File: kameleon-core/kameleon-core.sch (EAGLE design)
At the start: 38 parts, among them CN1 USB, CN3 LEFT, CN4 RIGHT, CN5 SWD, IC3 STM32F411CE/UFQFPN48, IC4 AP2112K-3.3TRG1, SW1 NRST, SW2 BTN, Y1 8MHz

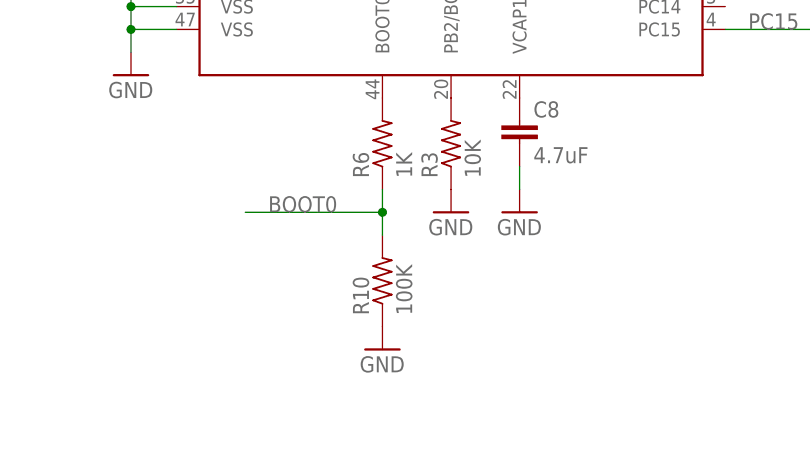
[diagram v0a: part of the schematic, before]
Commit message: Change R10 value to 10K
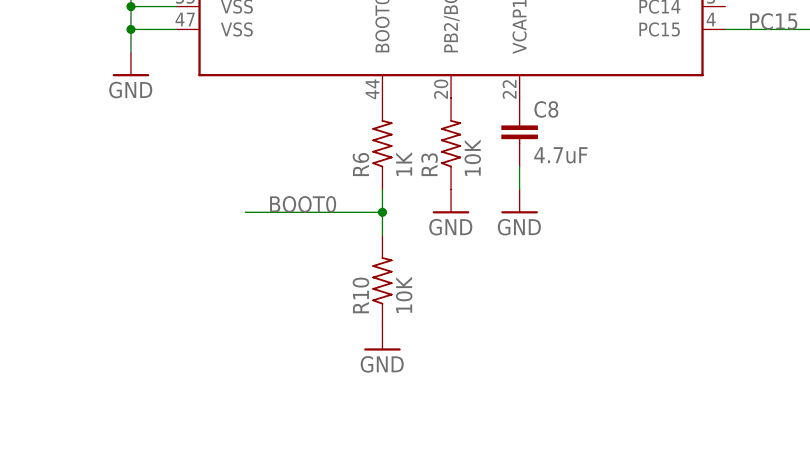
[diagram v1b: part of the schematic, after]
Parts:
- R10: value 100K -> 10K
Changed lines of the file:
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@@
 <part name="+3V1" library="supply1" deviceset="+3V3" device=""/>
 <part name="R6" library="Kameleon" deviceset="RES" device="" value="1K"/>
-<part name="R10" library="Kameleon" deviceset="RES" device="" value="100K"/>
+<part name="R10" library="Kameleon" deviceset="RES" device="" value="10K"/>
 <part name="GND2" library="supply1" deviceset="GND" device=""/>
 <part name="R3" library="Kameleon" deviceset="RES" device="" value="10K"/>

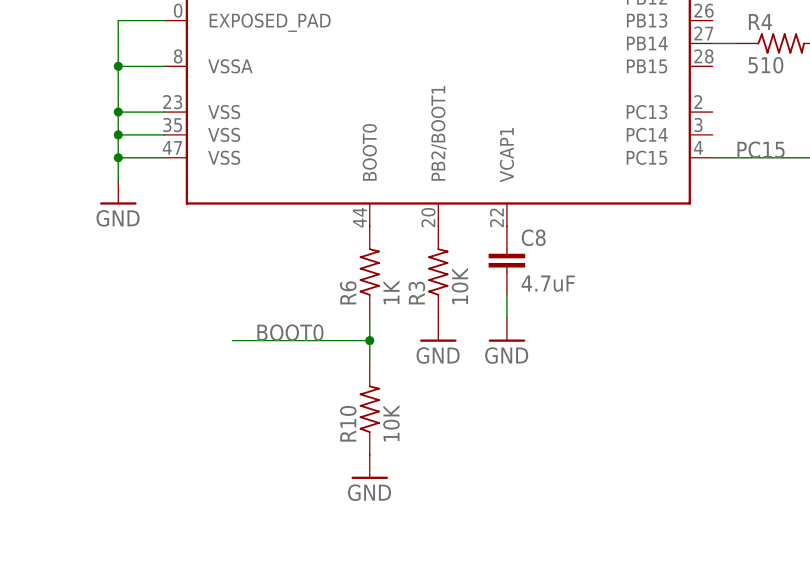
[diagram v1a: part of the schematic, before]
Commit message: Remove R3 and R6 because it's not needed
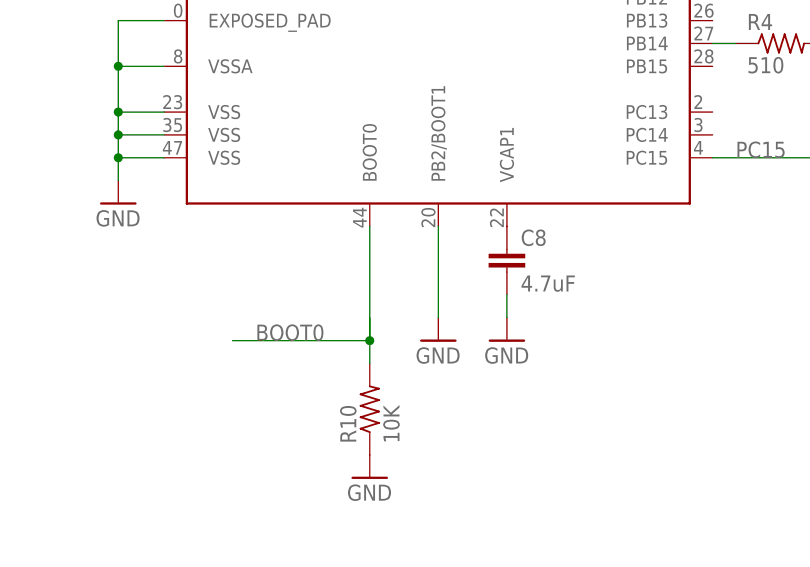
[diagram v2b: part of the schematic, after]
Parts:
- removed R3: 10K, Kameleon:RES
- removed R6: 1K, Kameleon:RES
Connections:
- removed net N$1: IC3.BOOT0, R6.2
- removed net N$2: IC3.PB2/BOOT1, R3.2
- net BOOT0: now also IC3.BOOT0; no longer R6.1
- net GND: now also IC3.PB2/BOOT1; no longer R3.1
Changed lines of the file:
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@@
 <part name="GND1" library="supply1" deviceset="GND" device=""/>
 <part name="+3V1" library="supply1" deviceset="+3V3" device=""/>
-<part name="R6" library="Kameleon" deviceset="RES" device="" value="1K"/>
 <part name="R10" library="Kameleon" deviceset="RES" device="" value="10K"/>
 <part name="GND2" library="supply1" deviceset="GND" device=""/>
-<part name="R3" library="Kameleon" deviceset="RES" device="" value="10K"/>
 <part name="GND3" library="supply1" deviceset="GND" device=""/>
 <part name="GND4" library="supply1" deviceset="GND" device=""/>
@@
 <attribute name="VALUE" x="38.1" y="134.62" size="1.778" layer="96" rot="R90"/>
 </instance>
-<instance part="R6" gate="G$1" x="68.58" y="35.56" smashed="yes" rot="R90">
-<attribute name="NAME" x="67.0814" y="31.75" size="1.778" layer="95" rot="R90"/>
-<attribute name="VALUE" x="71.882" y="31.75" size="1.778" layer="96" rot="R90"/>
-</instance>
 <instance part="R10" gate="G$1" x="68.58" y="20.32" smashed="yes" rot="R90">
 <attribute name="NAME" x="67.0814" y="16.51" size="1.778" layer="95" rot="R90"/>
@@
 <instance part="GND2" gate="1" x="68.58" y="12.7" smashed="yes">
 <attribute name="VALUE" x="66.04" y="10.16" size="1.778" layer="96"/>
-</instance>
-<instance part="R3" gate="G$1" x="76.2" y="35.56" smashed="yes" rot="R90">
-<attribute name="NAME" x="74.7014" y="31.75" size="1.778" layer="95" rot="R90"/>
-<attribute name="VALUE" x="79.502" y="31.75" size="1.778" layer="96" rot="R90"/>
 </instance>
 <instance part="GND3" gate="1" x="76.2" y="27.94" smashed="yes">
@@
 </segment>
 <segment>
-<pinref part="R3" gate="G$1" pin="1"/>
-<pinref part="GND3" gate="1" pin="GND"/>
-</segment>
-<segment>
 <pinref part="GND4" gate="1" pin="GND"/>
 <pinref part="C8" gate="G$1" pin="2"/>
@@
 <pinref part="GND22" gate="1" pin="GND"/>
 </segment>
-</net>
-<net name="N$1" class="0">
-<segment>
-<pinref part="IC3" gate="G$1" pin="BOOT0"/>
-<pinref part="R6" gate="G$1" pin="2"/>
+<segment>
+<pinref part="GND3" gate="1" pin="GND"/>
+<pinref part="IC3" gate="G$1" pin="PB2/BOOT1"/>
+<wire x1="76.2" y1="30.48" x2="76.2" y2="40.64" width="0.1524" layer="91"/>
 </segment>
 </net>
 <net name="BOOT0" class="0">
 <segment>
-<pinref part="R6" gate="G$1" pin="1"/>
 <pinref part="R10" gate="G$1" pin="2"/>
 <wire x1="68.58" y1="25.4" x2="68.58" y2="27.94" width="0.1524" layer="91"/>
@@
 <junction x="68.58" y="27.94"/>
 <label x="55.88" y="27.94" size="1.778" layer="95"/>
+<pinref part="IC3" gate="G$1" pin="BOOT0"/>
+<wire x1="68.58" y1="27.94" x2="68.58" y2="40.64" width="0.1524" layer="91"/>
 </segment>
 <segment>
@@
 </segment>
 </net>
-<net name="N$2" class="0">
-<segment>
-<pinref part="IC3" gate="G$1" pin="PB2/BOOT1"/>
-<pinref part="R3" gate="G$1" pin="2"/>
-</segment>
-</net>

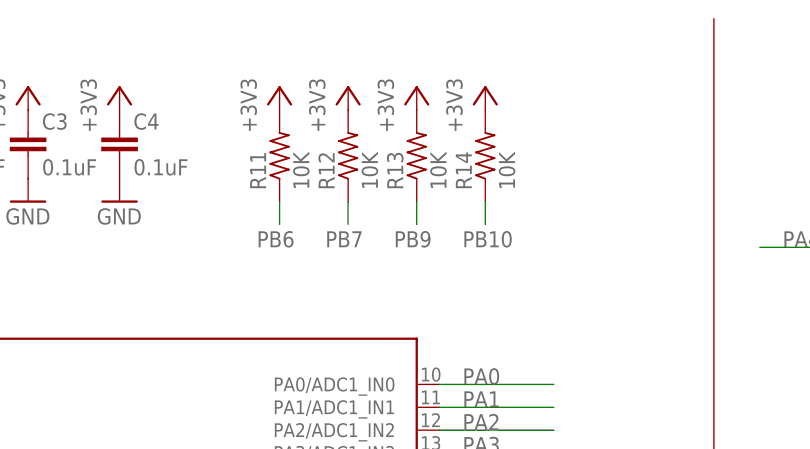
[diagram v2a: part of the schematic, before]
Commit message: I2C pull-ups are changed from 10K to NC
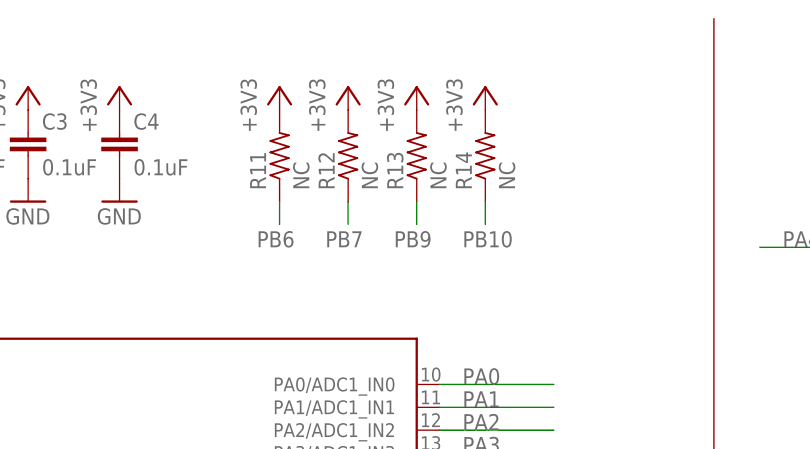
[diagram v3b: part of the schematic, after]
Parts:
- R11, R12, R13, R14: value 10K -> NC
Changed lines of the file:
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@@
 <part name="R9" library="Kameleon" deviceset="RES" device="" value="22"/>
 <part name="R8" library="Kameleon" deviceset="RES" device="" value="22"/>
-<part name="R11" library="Kameleon" deviceset="RES" device="" value="10K"/>
-<part name="R12" library="Kameleon" deviceset="RES" device="" value="10K"/>
-<part name="R13" library="Kameleon" deviceset="RES" device="" value="10K"/>
-<part name="R14" library="Kameleon" deviceset="RES" device="" value="10K"/>
+<part name="R11" library="Kameleon" deviceset="RES" device="" value="NC"/>
+<part name="R12" library="Kameleon" deviceset="RES" device="" value="NC"/>
+<part name="R13" library="Kameleon" deviceset="RES" device="" value="NC"/>
+<part name="R14" library="Kameleon" deviceset="RES" device="" value="NC"/>
 <part name="+3V10" library="supply1" deviceset="+3V3" device=""/>
 <part name="+3V11" library="supply1" deviceset="+3V3" device=""/>

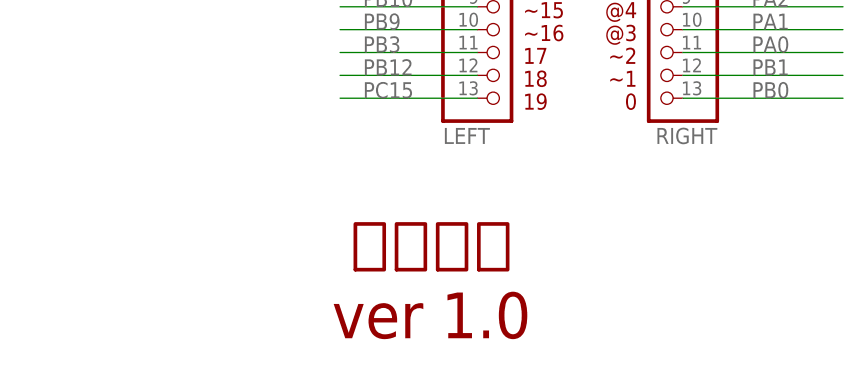
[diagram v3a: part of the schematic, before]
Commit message: Board name changed in English Version is changed to 1.0.0
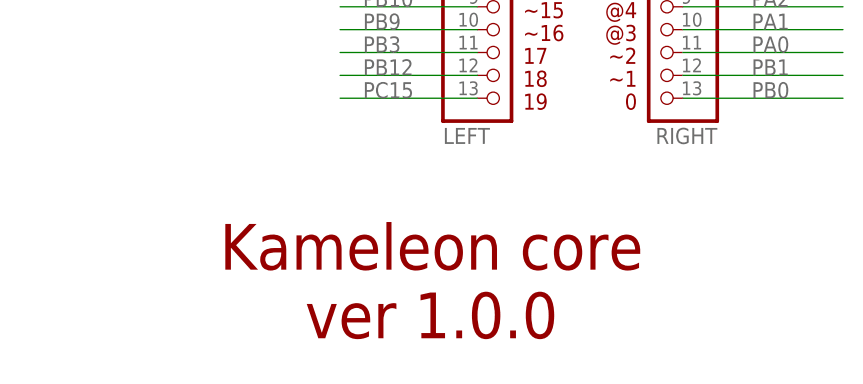
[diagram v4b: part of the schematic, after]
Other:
- note added: "Kameleon core ver 1.0.0"
- note removed: "카멜레온 ver 1.0"
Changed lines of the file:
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@@
 18
 19</text>
-<text x="187.96" y="12.7" size="5.08" layer="94" align="center">카멜레온
-ver 1.0</text>
+<text x="187.96" y="12.7" size="5.08" layer="94" align="center">Kameleon core
+ver 1.0.0</text>
 </plain>
 <instances>
